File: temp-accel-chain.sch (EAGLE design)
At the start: 7 parts, among them U1 ADT7420UCPZ-R2

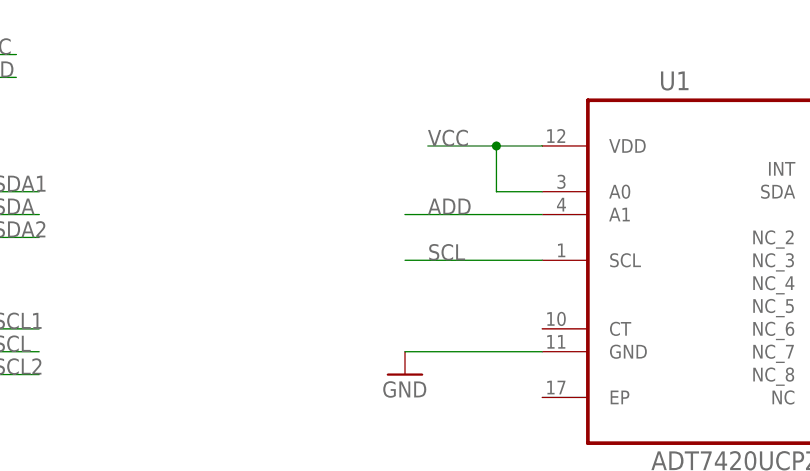
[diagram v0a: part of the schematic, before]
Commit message: added 10ks to adress lines
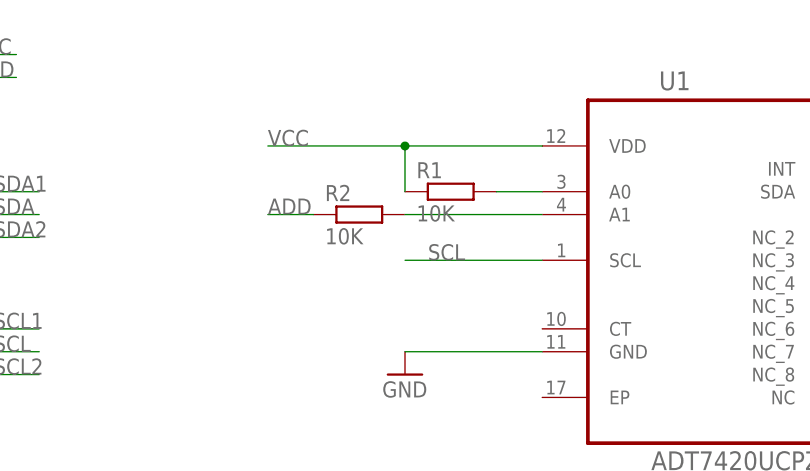
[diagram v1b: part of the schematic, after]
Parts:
- added R1, R2: 10K, resistor:R-EU_R0603
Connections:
- new net N$1: R1.2, U1.A0
- new net N$3: R2.2, U1.A1
- net ADD: now also R2.1; no longer U1.A1
- net VCC: now also R1.1; no longer U1.A0
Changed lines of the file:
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@@
 <part name="JP5" library="SparkFun-Passives" deviceset="JUMPER-3" device="SMD"/>
 <part name="GND4" library="supply1" deviceset="GND" device=""/>
+<part name="R1" library="resistor" deviceset="R-EU_" device="R0603" value="10K"/>
+<part name="R2" library="resistor" deviceset="R-EU_" device="R0603" value="10K"/>
 </parts>
 <sheets>
@@
 <instance part="JP5" gate="G$1" x="0" y="83.82" rot="R90"/>
 <instance part="GND4" gate="1" x="2.54" y="81.28"/>
+<instance part="R1" gate="G$1" x="63.5" y="73.66"/>
+<instance part="R2" gate="G$1" x="53.34" y="71.12"/>
 </instances>
 <busses>
@@
 <segment>
 <pinref part="U1" gate="A" pin="VDD"/>
-<wire x1="73.66" y1="78.74" x2="68.58" y2="78.74" width="0.1524" layer="91"/>
-<label x="60.96" y="78.74" size="1.778" layer="95"/>
-<pinref part="U1" gate="A" pin="A0"/>
-<wire x1="68.58" y1="78.74" x2="60.96" y2="78.74" width="0.1524" layer="91"/>
-<wire x1="73.66" y1="73.66" x2="68.58" y2="73.66" width="0.1524" layer="91"/>
-<wire x1="68.58" y1="73.66" x2="68.58" y2="78.74" width="0.1524" layer="91"/>
-<junction x="68.58" y="78.74"/>
+<label x="43.18" y="78.74" size="1.778" layer="95"/>
+<wire x1="73.66" y1="78.74" x2="58.42" y2="78.74" width="0.1524" layer="91"/>
+<pinref part="R1" gate="G$1" pin="1"/>
+<wire x1="58.42" y1="78.74" x2="43.18" y2="78.74" width="0.1524" layer="91"/>
+<wire x1="58.42" y1="73.66" x2="58.42" y2="78.74" width="0.1524" layer="91"/>
+<junction x="58.42" y="78.74"/>
 </segment>
 <segment>
@@
 <net name="ADD" class="0">
 <segment>
-<pinref part="U1" gate="A" pin="A1"/>
-<wire x1="73.66" y1="71.12" x2="58.42" y2="71.12" width="0.1524" layer="91"/>
-<label x="60.96" y="71.12" size="1.778" layer="95"/>
-</segment>
-<segment>
 <pinref part="JP5" gate="G$1" pin="2"/>
 <wire x1="2.54" y1="86.36" x2="15.24" y2="86.36" width="0.1524" layer="91"/>
 <label x="10.16" y="86.36" size="1.778" layer="95"/>
 </segment>
+<segment>
+<pinref part="R2" gate="G$1" pin="1"/>
+<wire x1="48.26" y1="71.12" x2="43.18" y2="71.12" width="0.1524" layer="91"/>
+<label x="43.18" y="71.12" size="1.778" layer="95"/>
+</segment>
 </net>
+<net name="N$1" class="0">
+<segment>
+<pinref part="U1" gate="A" pin="A0"/>
+<wire x1="73.66" y1="73.66" x2="68.58" y2="73.66" width="0.1524" layer="91"/>
+<pinref part="R1" gate="G$1" pin="2"/>
+</segment>
+</net>
+<net name="N$3" class="0">
+<segment>
+<pinref part="R2" gate="G$1" pin="2"/>
+<pinref part="U1" gate="A" pin="A1"/>
+<wire x1="58.42" y1="71.12" x2="73.66" y2="71.12" width="0.1524" layer="91"/>
+</segment>
+</net>

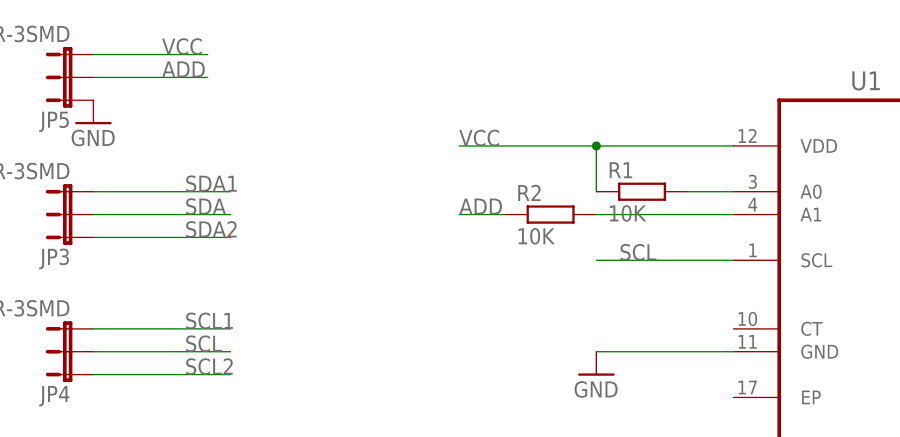
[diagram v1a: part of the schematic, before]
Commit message: temp i2c address either 00 or 11 thus saving a resistor
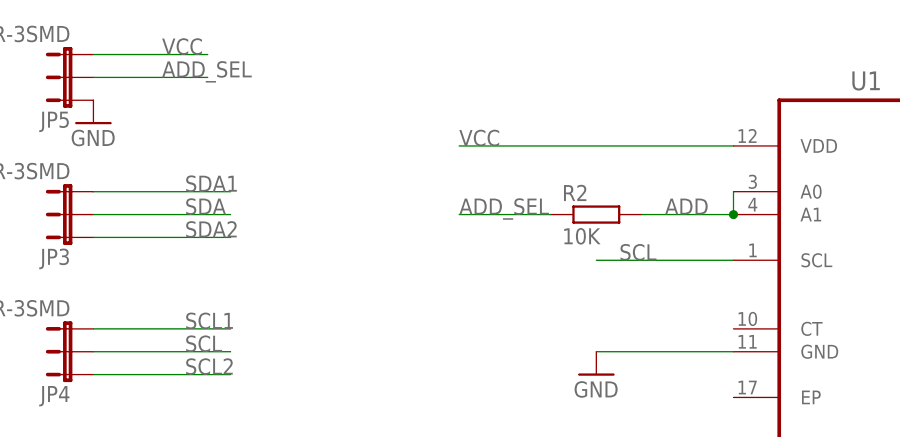
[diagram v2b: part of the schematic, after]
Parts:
- removed R1: 10K, resistor:R-EU_R0603
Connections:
- removed net N$1: R1.2, U1.A0
- removed net N$3: R2.2, U1.A1
- new net ADD_SEL: JP5.2, R2.1
- net ADD: now also R2.2, U1.A0, U1.A1; no longer JP5.2, R2.1
- net VCC: no longer R1.1
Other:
- moved on the sheet: R2
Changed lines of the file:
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@@
 <part name="JP5" library="SparkFun-Passives" deviceset="JUMPER-3" device="SMD"/>
 <part name="GND4" library="supply1" deviceset="GND" device=""/>
-<part name="R1" library="resistor" deviceset="R-EU_" device="R0603" value="10K"/>
 <part name="R2" library="resistor" deviceset="R-EU_" device="R0603" value="10K"/>
 </parts>
@@
 <instance part="JP5" gate="G$1" x="0" y="83.82" rot="R90"/>
 <instance part="GND4" gate="1" x="2.54" y="81.28"/>
-<instance part="R1" gate="G$1" x="63.5" y="73.66"/>
-<instance part="R2" gate="G$1" x="53.34" y="71.12"/>
+<instance part="R2" gate="G$1" x="58.42" y="71.12"/>
 </instances>
 <busses>
@@
 <pinref part="U1" gate="A" pin="VDD"/>
 <label x="43.18" y="78.74" size="1.778" layer="95"/>
-<wire x1="73.66" y1="78.74" x2="58.42" y2="78.74" width="0.1524" layer="91"/>
-<pinref part="R1" gate="G$1" pin="1"/>
-<wire x1="58.42" y1="78.74" x2="43.18" y2="78.74" width="0.1524" layer="91"/>
-<wire x1="58.42" y1="73.66" x2="58.42" y2="78.74" width="0.1524" layer="91"/>
-<junction x="58.42" y="78.74"/>
+<wire x1="73.66" y1="78.74" x2="43.18" y2="78.74" width="0.1524" layer="91"/>
 </segment>
 <segment>
@@
 <net name="ADD" class="0">
 <segment>
+<pinref part="R2" gate="G$1" pin="2"/>
+<pinref part="U1" gate="A" pin="A1"/>
+<wire x1="63.5" y1="71.12" x2="73.66" y2="71.12" width="0.1524" layer="91"/>
+<pinref part="U1" gate="A" pin="A0"/>
+<wire x1="73.66" y1="73.66" x2="73.66" y2="71.12" width="0.1524" layer="91"/>
+<junction x="73.66" y="71.12"/>
+<label x="66.04" y="71.12" size="1.778" layer="95"/>
+</segment>
+</net>
+<net name="ADD_SEL" class="0">
+<segment>
+<pinref part="R2" gate="G$1" pin="1"/>
+<wire x1="53.34" y1="71.12" x2="43.18" y2="71.12" width="0.1524" layer="91"/>
+<label x="43.18" y="71.12" size="1.778" layer="95"/>
+</segment>
+<segment>
 <pinref part="JP5" gate="G$1" pin="2"/>
 <wire x1="2.54" y1="86.36" x2="15.24" y2="86.36" width="0.1524" layer="91"/>
 <label x="10.16" y="86.36" size="1.778" layer="95"/>
 </segment>
-<segment>
-<pinref part="R2" gate="G$1" pin="1"/>
-<wire x1="48.26" y1="71.12" x2="43.18" y2="71.12" width="0.1524" layer="91"/>
-<label x="43.18" y="71.12" size="1.778" layer="95"/>
-</segment>
 </net>
-<net name="N$1" class="0">
-<segment>
-<pinref part="U1" gate="A" pin="A0"/>
-<wire x1="73.66" y1="73.66" x2="68.58" y2="73.66" width="0.1524" layer="91"/>
-<pinref part="R1" gate="G$1" pin="2"/>
-</segment>
-</net>
-<net name="N$3" class="0">
-<segment>
-<pinref part="R2" gate="G$1" pin="2"/>
-<pinref part="U1" gate="A" pin="A1"/>
-<wire x1="58.42" y1="71.12" x2="73.66" y2="71.12" width="0.1524" layer="91"/>
-</segment>
-</net>

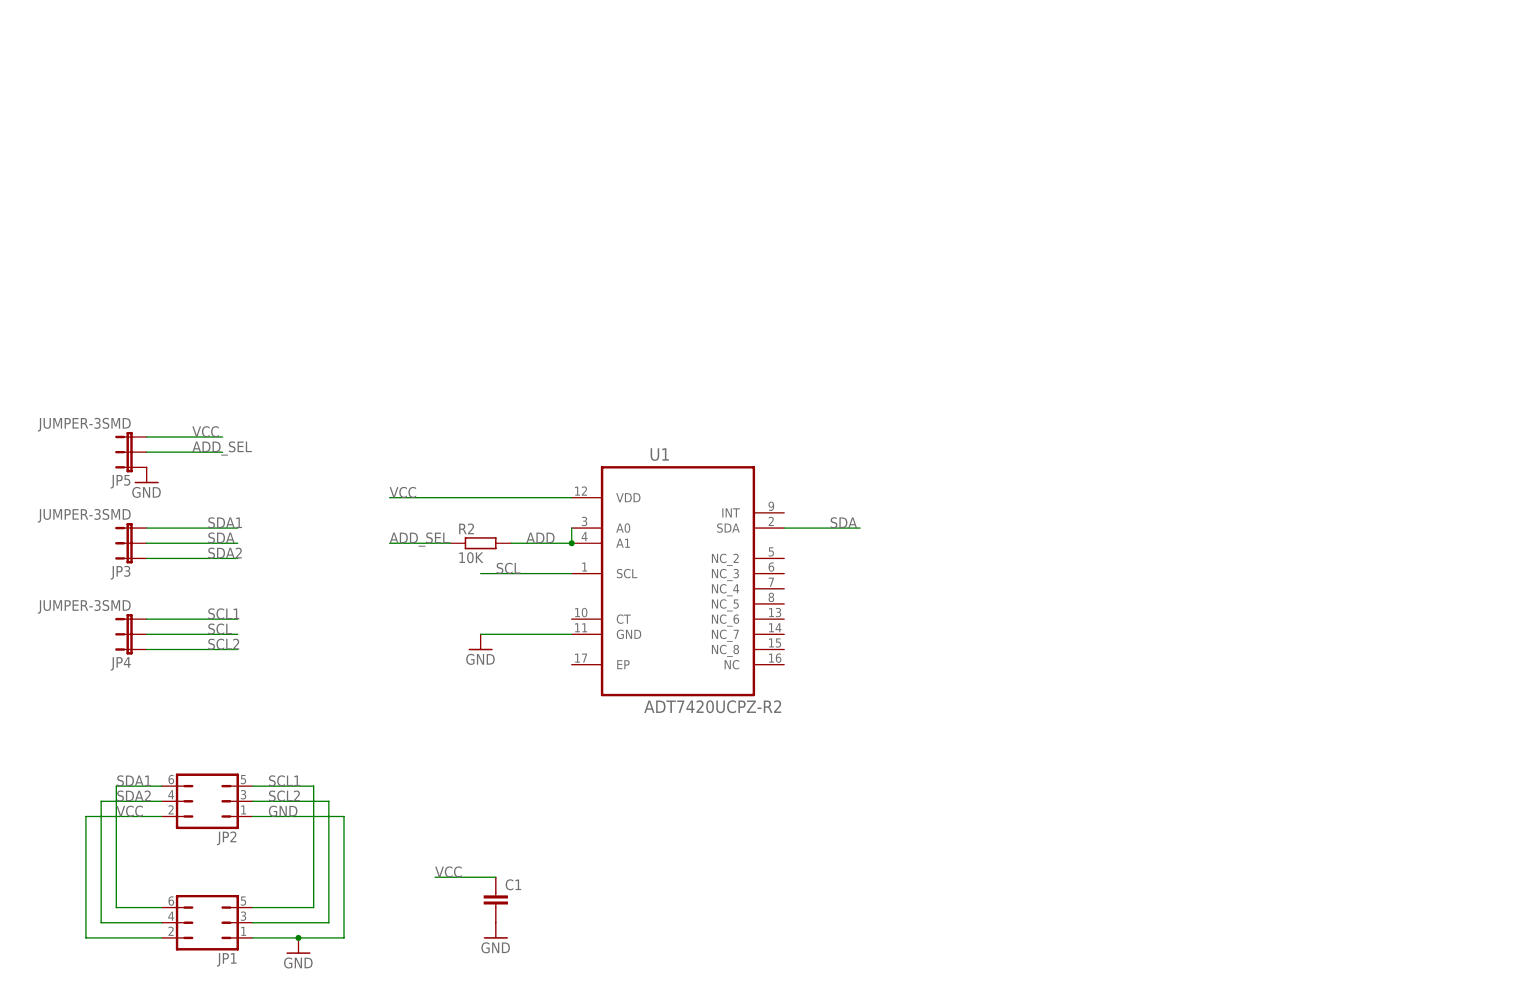
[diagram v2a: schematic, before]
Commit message: added accel to back and mostly routed
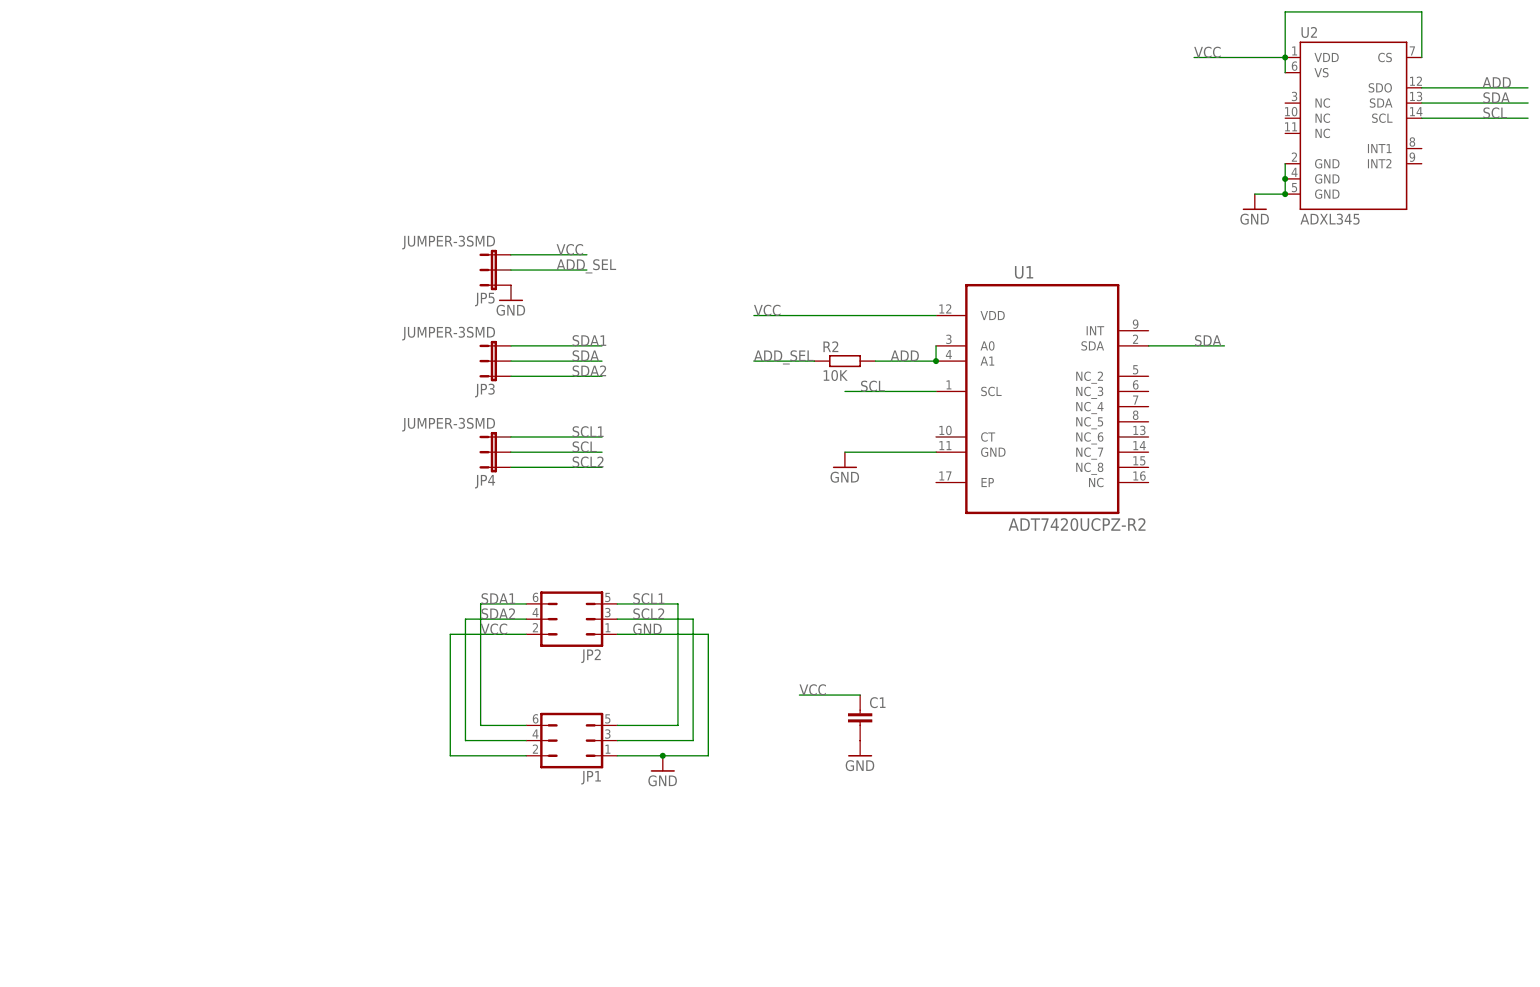
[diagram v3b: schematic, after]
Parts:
- added U2: ADXL345, SparkFun-Sensors:ADXL345
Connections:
- net ADD: now also U2.SDO
- net GND: now also U2.GND@2, U2.GND@4, U2.GND@5
- net SCL: now also U2.SCL
- net SDA: now also U2.SDA
- net VCC: now also U2.CS, U2.VDD, U2.VS
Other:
- moved on the sheet: C1, JP1, JP2, JP3, JP4, JP5, R2, U1

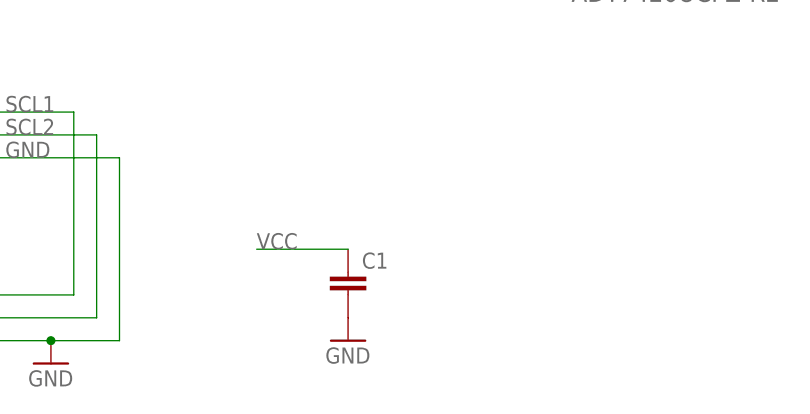
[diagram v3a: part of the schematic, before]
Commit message: completely routed board
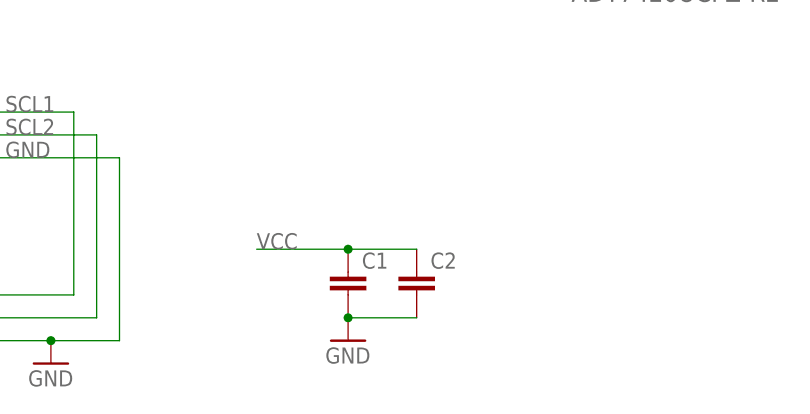
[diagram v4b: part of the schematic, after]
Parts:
- added C2: (no value), resistor:C-EUC0805
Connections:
- net GND: now also C2.2
- net VCC: now also C2.1
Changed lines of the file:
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@@
 <part name="U2" library="SparkFun-Sensors" deviceset="ADXL345" device=""/>
 <part name="GND5" library="supply1" deviceset="GND" device=""/>
+<part name="C2" library="resistor" deviceset="C-EU" device="C0805"/>
 </parts>
 <sheets>
@@
 <instance part="U2" gate="G$1" x="203.2" y="142.24"/>
 <instance part="GND5" gate="1" x="187.96" y="127"/>
+<instance part="C2" gate="G$1" x="129.54" y="43.18"/>
 </instances>
 <busses>
@@
 <wire x1="121.92" y1="45.72" x2="111.76" y2="45.72" width="0.1524" layer="91"/>
 <label x="111.76" y="45.72" size="1.778" layer="95"/>
+<pinref part="C2" gate="G$1" pin="1"/>
+<wire x1="129.54" y1="45.72" x2="121.92" y2="45.72" width="0.1524" layer="91"/>
+<junction x="121.92" y="45.72"/>
 </segment>
 <segment>
@@
 <pinref part="C1" gate="G$1" pin="2"/>
 <pinref part="GND2" gate="1" pin="GND"/>
+<pinref part="C2" gate="G$1" pin="2"/>
+<wire x1="121.92" y1="38.1" x2="129.54" y2="38.1" width="0.1524" layer="91"/>
+<junction x="121.92" y="38.1"/>
 </segment>
 <segment>
